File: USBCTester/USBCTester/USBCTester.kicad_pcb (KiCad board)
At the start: 4 copper layers, 114.9 x 92.1 mm, 59 parts, among them J1 AUSB1-DFN-PTR3, J2 AUSB1-DFN-PTR3, U1 74HC595, U2 74HC595, U3 74HC595, U4 74HC595, U5 74HC595, U6 74HC595, U7 RaspberryPi_Pico

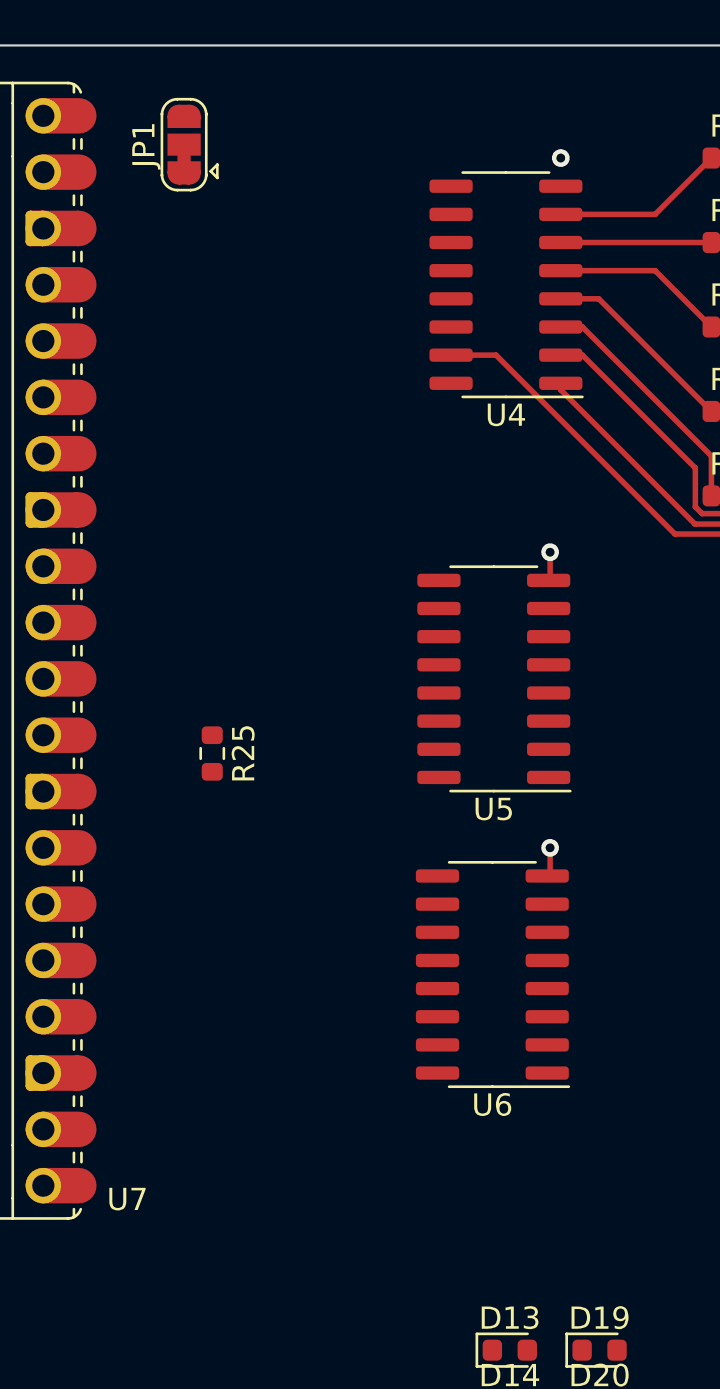
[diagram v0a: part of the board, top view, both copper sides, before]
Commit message: add power plane and vias for high current and decoupling caps
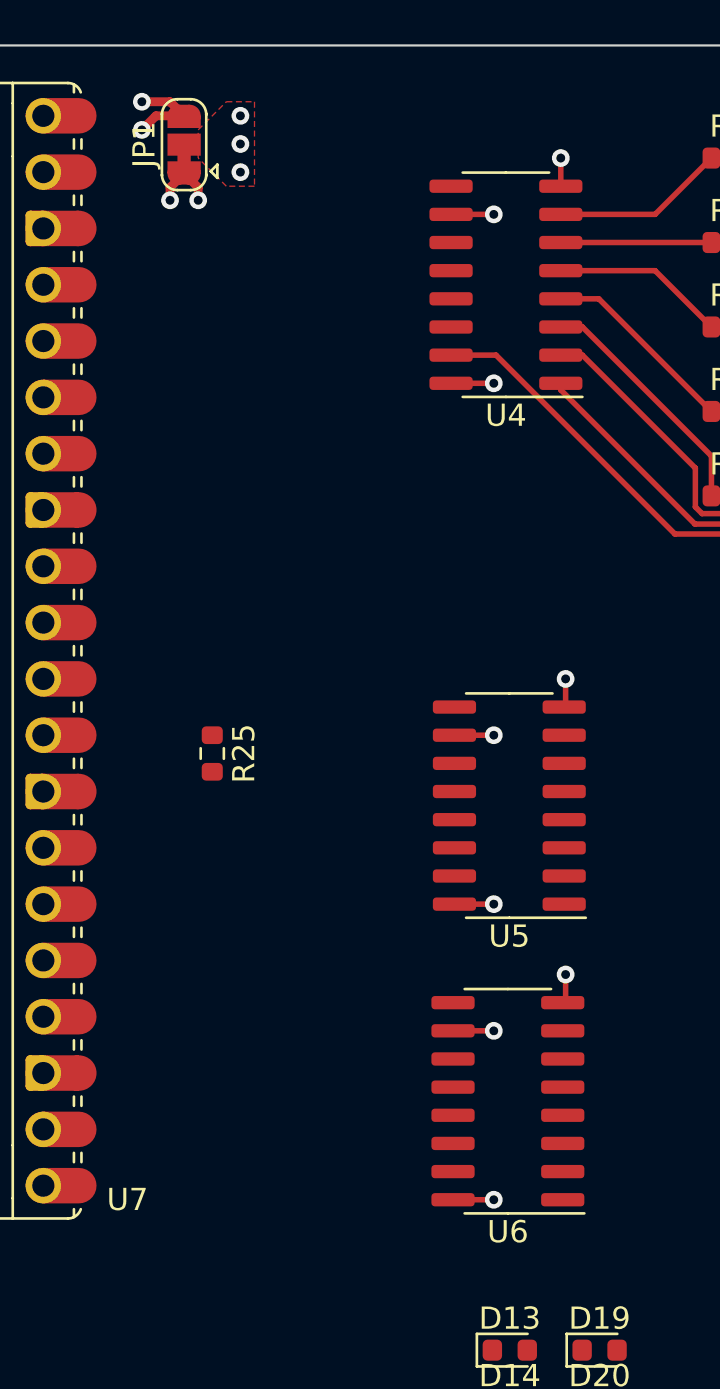
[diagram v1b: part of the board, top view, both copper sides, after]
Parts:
- moved U6 5.76 mm to (182.2, 109.2)
- moved U5 5.76 mm to (182.3, 95.9)
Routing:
- net VCC: track 0.00 -> 11.6 mm, vias 0 -> 9
- net VBUS: track 0.00 -> 4.34 mm, vias 0 -> 2
- net +3V3: track 0.00 -> 2.95 mm, vias 0 -> 2
- net GND: track 27.4 -> 28.7 mm
- added copper zone on In2.Cu, net +3V3
- added copper zone on In2.Cu, net VBUS
- added copper zone on F.Cu, net VCC
- added copper zone on In2.Cu, net VCC
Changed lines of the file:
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@@
   )
   (footprint "Package_SO:SOIC-16_3.9x9.9mm_P1.27mm" (layer "F.Cu")
-    (at 181.61 90.17 180)
+    (at 182.31 95.885 180)
     (descr "SOIC, 16 Pin (JEDEC MS-012AC, https://www.analog.com/media/en/package-pcb-resources/package/pkg_pdf/soic_narrow-r/r_16.pdf), generated with kicad-footprint-generator ipc_gullwing_generator.py")
     (tags "SOIC SO")
@@
   )
   (footprint "Package_SO:SOIC-16_3.9x9.9mm_P1.27mm" (layer "F.Cu")
-    (at 181.545 103.505 180)
+    (at 182.245 109.22 180)
     (descr "SOIC, 16 Pin (JEDEC MS-012AC, https://www.analog.com/media/en/package-pcb-resources/package/pkg_pdf/soic_narrow-r/r_16.pdf), generated with kicad-footprint-generator ipc_gullwing_generator.py")
     (tags "SOIC SO")
@@
   (segment (start 195.275 70.485) (end 193.0775 70.485) (width 0.25) (layer "F.Cu") (net 7))
   (segment (start 193.0775 66.675) (end 195.275 66.675) (width 0.25) (layer "F.Cu") (net 8))
-  (segment (start 184.15 85.66) (end 184.085 85.725) (width 0.25) (layer "F.Cu") (net 17))
+  (segment (start 184.85 91.375) (end 184.785 91.44) (width 0.25) (layer "F.Cu") (net 17))
+  (segment (start 184.6325 66.675) (end 184.6325 67.945) (width 0.25) (layer "F.Cu") (net 17))
   (segment (start 196.85 81.915) (end 196.85 78.105) (width 0.25) (layer "F.Cu") (net 17))
   (segment (start 196.85 70.485) (end 196.85 73.025) (width 0.25) (layer "F.Cu") (net 17))
-  (segment (start 184.15 98.93) (end 184.02 99.06) (width 0.25) (layer "F.Cu") (net 17))
+  (segment (start 184.85 104.645) (end 184.72 104.775) (width 0.25) (layer "F.Cu") (net 17))
   (segment (start 196.85 70.485) (end 196.85 66.675) (width 0.25) (layer "F.Cu") (net 17))
   (segment (start 210.5275 69.85) (end 210.5275 72.3525) (width 0.25) (layer "F.Cu") (net 17))
-  (segment (start 184.15 84.455) (end 184.15 85.66) (width 0.25) (layer "F.Cu") (net 17))
-  (segment (start 184.15 97.79) (end 184.15 98.93) (width 0.25) (layer "F.Cu") (net 17))
+  (segment (start 184.85 90.17) (end 184.85 91.375) (width 0.25) (layer "F.Cu") (net 17))
+  (segment (start 184.85 103.505) (end 184.85 104.645) (width 0.25) (layer "F.Cu") (net 17))
   (segment (start 210.565 72.39) (end 210.5275 72.4275) (width 0.25) (layer "F.Cu") (net 17))
   (segment (start 210.5275 72.3525) (end 210.565 72.39) (width 0.25) (layer "F.Cu") (net 17))
@@
   (segment (start 210.5275 72.4275) (end 210.5275 79.375) (width 0.25) (layer "F.Cu") (net 17))
   (via (at 210.565 72.39) (size 0.8) (drill 0.4) (layers "F.Cu" "B.Cu") (free) (net 17))
-  (via (at 184.15 97.79) (size 0.8) (drill 0.4) (layers "F.Cu" "B.Cu") (free) (net 17))
+  (via (at 184.85 103.505) (size 0.8) (drill 0.4) (layers "F.Cu" "B.Cu") (free) (net 17))
   (via (at 184.6325 66.675) (size 0.8) (drill 0.4) (layers "F.Cu" "B.Cu") (free) (net 17))
-  (via (at 184.15 84.455) (size 0.8) (drill 0.4) (layers "F.Cu" "B.Cu") (free) (net 17))
+  (via (at 184.85 90.17) (size 0.8) (drill 0.4) (layers "F.Cu" "B.Cu") (free) (net 17))
   (via (at 196.85 73.025) (size 0.8) (drill 0.4) (layers "F.Cu" "B.Cu") (net 17))
   (segment (start 200.845 83.635) (end 205.105 79.375) (width 0.25) (layer "F.Cu") (net 56))
@@
   (segment (start 191.4275 66.675) (end 188.8875 69.215) (width 0.25) (layer "F.Cu") (net 63))
   (segment (start 188.8875 69.215) (end 184.6325 69.215) (width 0.25) (layer "F.Cu") (net 63))
+  (segment (start 168.275 68.005) (end 167.64 67.37) (width 0.4) (layer "F.Cu") (net 97))
+  (segment (start 167.005 68.58) (end 167.005 68.005) (width 0.4) (layer "F.Cu") (net 97))
+  (segment (start 167.005 68.005) (end 167.64 67.37) (width 0.4) (layer "F.Cu") (net 97))
+  (segment (start 168.275 68.58) (end 168.275 68.005) (width 0.4) (layer "F.Cu") (net 97))
+  (via (at 167.005 68.58) (size 0.8) (drill 0.4) (layers "F.Cu" "B.Cu") (free) (net 97))
+  (via (at 168.275 68.58) (size 0.8) (drill 0.4) (layers "F.Cu" "B.Cu") (free) (net 97))
+  (segment (start 167.005 64.135) (end 167.64 64.77) (width 0.4) (layer "F.Cu") (net 113))
+  (segment (start 165.735 64.135) (end 167.005 64.135) (width 0.4) (layer "F.Cu") (net 113))
+  (segment (start 166.37 64.77) (end 167.64 64.77) (width 0.4) (layer "F.Cu") (net 113))
+  (segment (start 165.735 65.405) (end 166.37 64.77) (width 0.4) (layer "F.Cu") (net 113))
+  (via (at 165.735 65.405) (size 0.8) (drill 0.4) (layers "F.Cu" "B.Cu") (free) (net 113))
+  (via (at 165.735 64.135) (size 0.8) (drill 0.4) (layers "F.Cu" "B.Cu") (free) (net 113))
+  (segment (start 170.15 66.07) (end 170.18 66.04) (width 0.25) (layer "F.Cu") (net 118))
+  (segment (start 170.18 66.04) (end 170.21 66.07) (width 0.25) (layer "F.Cu") (net 118))
+  (segment (start 181.61 69.215) (end 179.6825 69.215) (width 0.25) (layer "F.Cu") (net 118))
+  (segment (start 181.61 113.665) (end 179.77 113.665) (width 0.25) (layer "F.Cu") (net 118))
+  (segment (start 179.6825 76.835) (end 181.61 76.835) (width 0.25) (layer "F.Cu") (net 118))
+  (segment (start 181.61 100.33) (end 179.835 100.33) (width 0.25) (layer "F.Cu") (net 118))
+  (segment (start 179.301592 69.215) (end 179.6825 69.215) (width 0.25) (layer "F.Cu") (net 118))
+  (segment (start 181.61 106.045) (end 179.77 106.045) (width 0.25) (layer "F.Cu") (net 118))
+  (segment (start 181.61 92.71) (end 179.835 92.71) (width 0.25) (layer "F.Cu") (net 118))
+  (via (at 170.18 66.04) (size 0.8) (drill 0.4) (layers "F.Cu" "B.Cu") (net 118))
+  (via (at 181.61 69.215) (size 0.8) (drill 0.4) (layers "F.Cu" "B.Cu") (free) (net 118))
+  (via (at 181.61 100.33) (size 0.8) (drill 0.4) (layers "F.Cu" "B.Cu") (free) (net 118))
+  (via (at 181.61 106.045) (size 0.8) (drill 0.4) (layers "F.Cu" "B.Cu") (free) (net 118))
+  (via (at 170.18 67.31) (size 0.8) (drill 0.4) (layers "F.Cu" "B.Cu") (free) (net 118))
+  (via (at 181.61 76.835) (size 0.8) (drill 0.4) (layers "F.Cu" "B.Cu") (free) (net 118))
+  (via (at 181.61 92.71) (size 0.8) (drill 0.4) (layers "F.Cu" "B.Cu") (free) (net 118))
+  (via (at 181.61 113.665) (size 0.8) (drill 0.4) (layers "F.Cu" "B.Cu") (free) (net 118))
+  (via (at 170.18 64.77) (size 0.8) (drill 0.4) (layers "F.Cu" "B.Cu") (free) (net 118))
+  (zone (net 118) (net_name "VCC") (layer "F.Cu") (name "VCC") (hatch edge 0.5)
+    (priority 4)
+    (connect_pads (clearance 0.5))
+    (min_thickness 0.25) (filled_areas_thickness no)
+    (fill yes (thermal_gap 0.5) (thermal_bridge_width 0.5))
+    (polygon
+      (pts
+        (xy 168.275 66.675)
+        (xy 168.275 65.405)
+        (xy 169.545 64.135)
+        (xy 170.815 64.135)
+        (xy 170.815 67.945)
+        (xy 169.545 67.945)
+      )
+    )
+  )
   (zone (net 17) (net_name "GND") (layer "In1.Cu") (name "GND") (hatch edge 0.5)
     (connect_pads (clearance 0.5))
@@
       )
     )
+  )
+  (zone (net 118) (net_name "VCC") (layer "In2.Cu") (name "VCC") (hatch edge 0.5)
+    (priority 1)
+    (connect_pads (clearance 0.5))
+    (min_thickness 0.25) (filled_areas_thickness no)
+    (fill yes (thermal_gap 0.5) (thermal_bridge_width 0.5))
+    (polygon
+      (pts
+        (xy 219.075 153.035)
+        (xy 105.41 153.035)
+        (xy 105.41 62.23)
+        (xy 219.075 62.23)
+      )
+    )
+    (polygon
+      (pts
+        (xy 160.02 63.5)
+        (xy 160.02 76.2)
+        (xy 168.91 76.2)
+        (xy 168.91 63.5)
+      )
+    )
+  )
+  (zone (net 113) (net_name "VBUS") (layer "In2.Cu") (name "VBUS") (hatch edge 0.5)
+    (priority 2)
+    (connect_pads (clearance 0.5))
+    (min_thickness 0.25) (filled_areas_thickness no)
+    (fill yes (thermal_gap 0.5) (thermal_bridge_width 0.5))
+    (polygon
+      (pts
+        (xy 168.91 63.5)
+        (xy 160.02 63.5)
+        (xy 160.02 66.04)
+        (xy 163.83 66.04)
+        (xy 167.005 66.04)
+        (xy 168.91 66.04)
+      )
+    )
+  )
+  (zone (net 97) (net_name "+3V3") (layer "In2.Cu") (name "3V3") (hatch edge 0.5)
+    (priority 3)
+    (connect_pads (clearance 0.5))
+    (min_thickness 0.25) (filled_areas_thickness no)
+    (fill yes (thermal_gap 0.5) (thermal_bridge_width 0.5))
+    (polygon
+      (pts
+        (xy 163.83 66.675)
+        (xy 163.83 73.66)
+        (xy 160.02 73.66)
+        (xy 160.02 76.2)
+        (xy 168.91 76.2)
+        (xy 168.91 66.675)
+      )
+    )

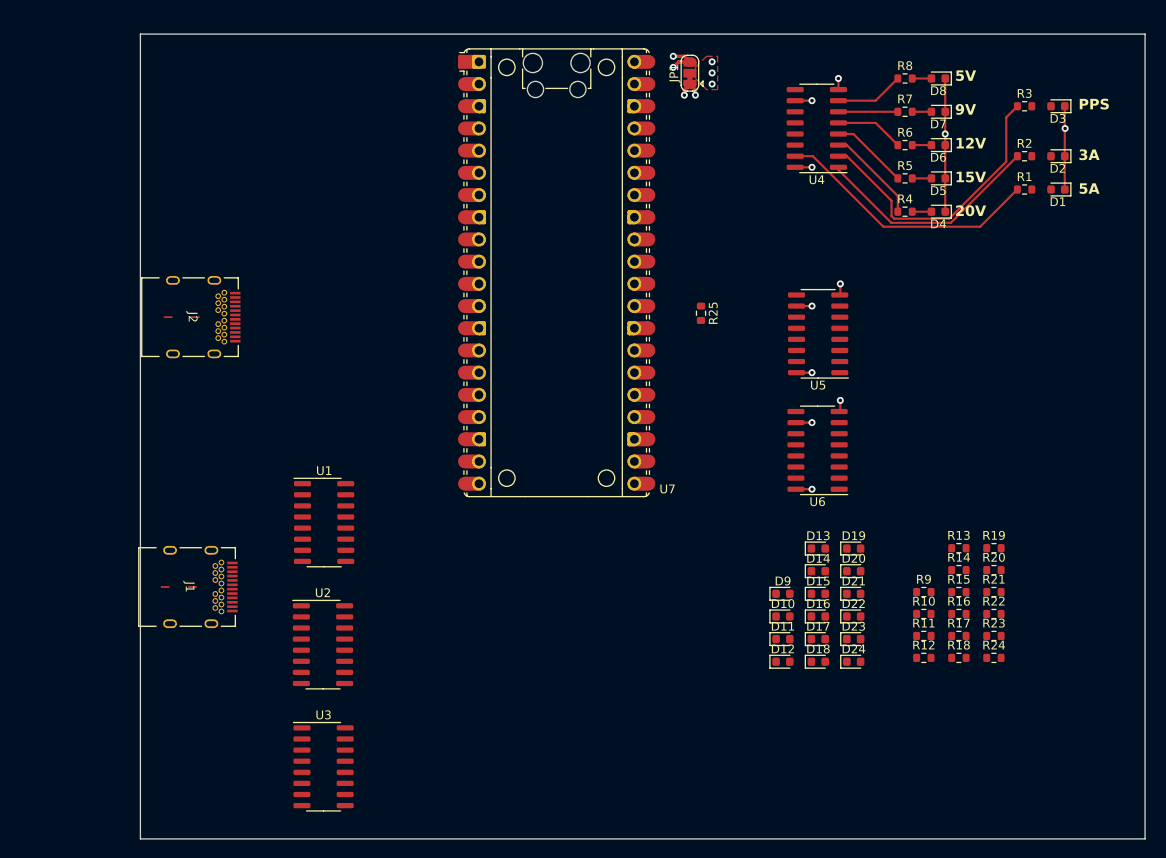
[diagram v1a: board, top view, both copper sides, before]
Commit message: continu wiring and add decoupling caps
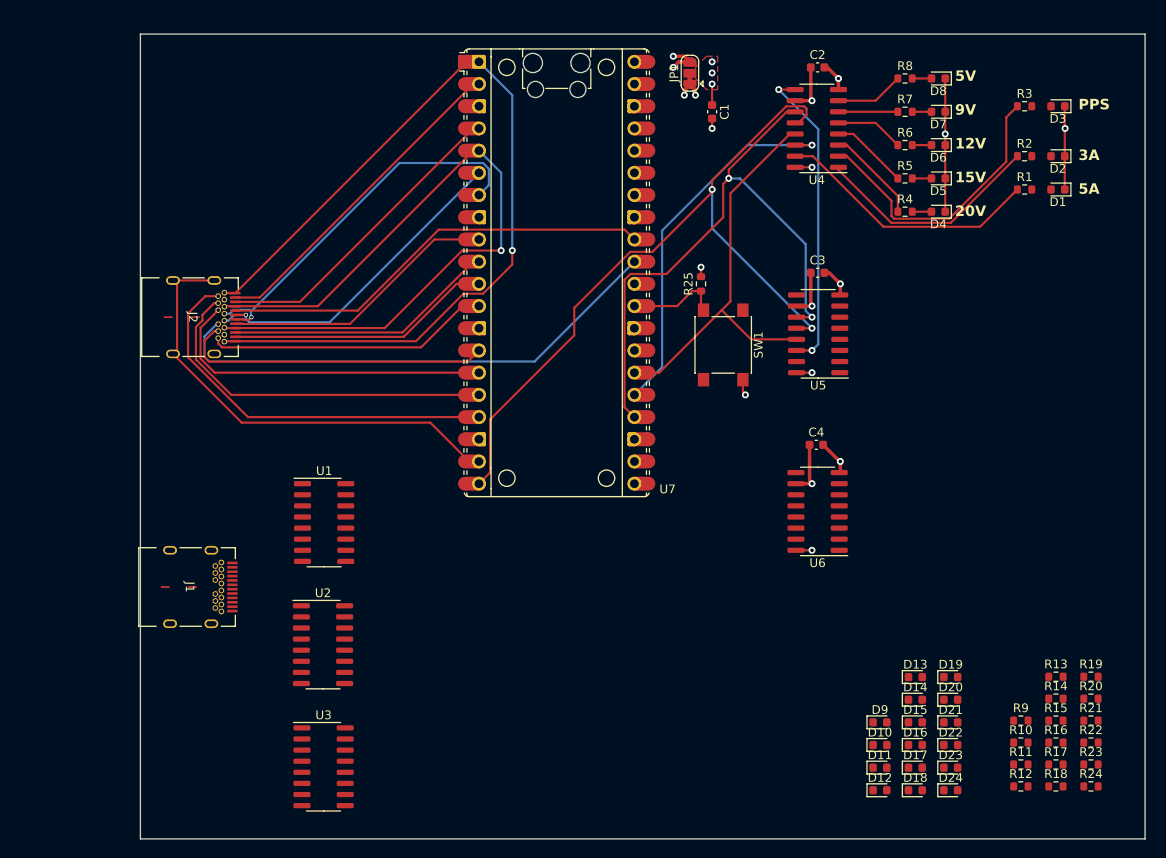
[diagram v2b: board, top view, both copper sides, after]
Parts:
- added C1: C, Capacitor_SMD:C_0603_1608Metric, F.Cu at (170.2, 70.5)
- added C2: C, Capacitor_SMD:C_0603_1608Metric, F.Cu at (182.2, 65.4)
- added C3: C, Capacitor_SMD:C_0603_1608Metric, F.Cu at (182.2, 88.9)
- added C4: C, Capacitor_SMD:C_0603_1608Metric, F.Cu at (182.1, 108.6)
- added SW1: SW_Push, Button_Switch_SMD:SW_Push_1P1T_NO_6x6mm_H9.5mm, F.Cu at (171.4, 97.2)
- moved D10 18.4 mm to (189.4, 142.9)
- moved D15 18.4 mm to (193.4, 140.3)
- moved D16 18.4 mm to (193.4, 142.9)
- moved D21 18.4 mm to (197.5, 140.3)
- moved D22 18.4 mm to (197.5, 142.9)
- moved D9 18.4 mm to (189.4, 140.3)
- moved R10 18.4 mm to (205.5, 142.6)
- moved R11 18.4 mm to (205.5, 145.2)
- moved R13 18.4 mm to (209.5, 135.1)
- moved R16 18.4 mm to (209.5, 142.6)
- moved R17 18.4 mm to (209.5, 145.2)
- moved R19 18.4 mm to (213.5, 135.1)
- moved R22 18.4 mm to (213.5, 142.6)
- moved R23 18.4 mm to (213.5, 145.2)
- moved D13 18.4 mm to (193.4, 135.2)
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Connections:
- U7 pad 20: unconnected-(U7-GPIO15-Pad20) -> RCLK
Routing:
- net TEST_CABLE_GROUND_IN: track 0.00 -> 101.5 mm, vias 0 -> 1
- net RCLK: track 0.00 -> 86.7 mm, vias 0 -> 2
- net TEST_CABLE_VBUS_IN: track 0.00 -> 84.4 mm, vias 0 -> 1
- net SRCLK: track 0.00 -> 68.8 mm, vias 0 -> 2
- net Net-(U7-GPIO26_ADC0): track 0.00 -> 58.6 mm
- net Net-(U7-GPIO14): track 0.00 -> 53.6 mm
- net Net-(U7-GPIO27_ADC1): track 0.00 -> 50.0 mm
- net Net-(U4-~{OE}): track 0.00 -> 46.9 mm
- net Net-(U7-GPIO13): track 0.00 -> 45.4 mm
- net Net-(U4-SER): track 0.00 -> 45.0 mm, vias 0 -> 1
- net TEST_CABLE_D-_IN: track 0.00 -> 44.0 mm, vias 0 -> 1
- net Net-(U7-GPIO12): track 0.00 -> 41.8 mm
- net Net-(U7-GPIO11): track 0.00 -> 38.9 mm
- net TEST_CABLE_D+_IN: track 0.00 -> 38.4 mm, vias 0 -> 1
- net Net-(U7-GPIO1): track 0.00 -> 38.0 mm
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
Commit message: organize usb2 and usb3 status leds
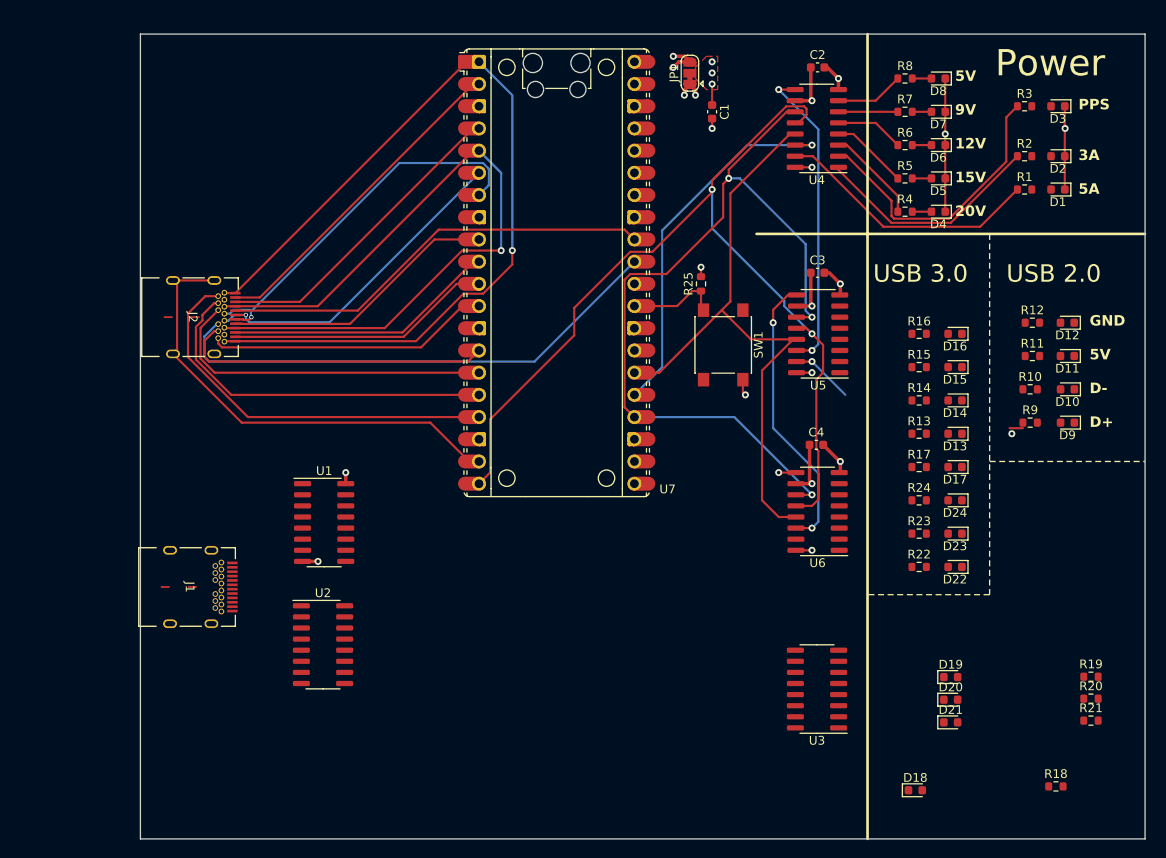
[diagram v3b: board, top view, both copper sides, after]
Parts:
- moved D12 57.6 mm to (210.8, 94.6), turned to 180 degrees
- moved U3 57.1 mm to (182.2, 136.5), turned to 180 degrees
- moved R12 53.1 mm to (206.8, 94.6)
- moved D11 51.7 mm to (210.8, 98.4), turned to 180 degrees
- moved R16 49.3 mm to (193.9, 95.9)
- moved D16 47.3 mm to (198.0, 95.9), turned to 180 degrees
- moved R11 46.7 mm to (206.8, 98.4)
- moved D10 46.0 mm to (210.8, 102.2), turned to 180 degrees
- moved R15 43.4 mm to (193.9, 99.7)
- moved D15 40.9 mm to (198.0, 99.7), turned to 180 degrees
- moved D9 40.4 mm to (210.8, 106.0), turned to 180 degrees
- moved R10 40.4 mm to (206.6, 102.2)
- moved R24 38.2 mm to (193.9, 114.9)
- moved R14 37.5 mm to (193.9, 103.5)
- moved R17 37.5 mm to (193.9, 111.1)
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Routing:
- net Net-(U5-QH'): track 0.00 -> 32.6 mm, vias 0 -> 2
- net SRCLK: track 68.8 -> 94.7 mm, vias 2 -> 3
- net Net-(U4-~{OE}): track 46.9 -> 71.8 mm
- net RCLK: track 86.7 -> 110.4 mm
- net Net-(U5-QA): track 0.00 -> 8.69 mm, vias 0 -> 2
- net Net-(U1-SER): track 0.00 -> 1.97 mm, vias 0 -> 1
- net GND: track 38.2 -> 39.9 mm, vias 7 -> 8
- net VCC: track 28.1 -> 29.4 mm, vias 10 -> 11
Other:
- board text added: "GND 5V D- D+"
- board text added: "Power"
- board text added: "TODO: add more LEDs for U3, to indicate CC/VCON status details and whether cable is reversed/absent"
- board text added: "USB 2.0"
- board text added: "USB 3.0"
